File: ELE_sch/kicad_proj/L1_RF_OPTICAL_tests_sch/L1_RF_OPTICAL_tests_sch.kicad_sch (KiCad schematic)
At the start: 0 parts

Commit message: update parts list, schematics diode placement
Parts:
- added D1: BPW34S, OptoDevice:Osram_BPW34S-SMD, symbol Sensor_Optical:BPW34-SMD
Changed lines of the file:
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@@
 	(generator_version "10.0")
 	(paper "A4")
+	(symbol
+		(lib_id "Sensor_Optical:BPW34-SMD")
+		(at 145.288 92.456 0)
+		(unit 1)
+		(body_style 1)
+		(exclude_from_sim no)
+		(in_bom yes)
+		(on_board yes)
+		(in_pos_files yes)
+		(dnp no)
+		(fields_autoplaced yes)
+		(property "Reference" "D1"
+			(at 144.3609 83.82 0)
+			(show_name no)
+			(do_not_autoplace no)
+			(effects
+				(font
+					(size 1.27 1.27)
+				)
+			)
+		)
+		(property "Value" "BPW34S"
+			(at 144.3609 86.36 0)
+			(show_name no)
+			(do_not_autoplace no)
+			(effects
+				(font
+					(size 1.27 1.27)
+				)
+			)
+		)
+		(property "Footprint" "OptoDevice:Osram_BPW34S-SMD"
+			(at 145.288 88.011 0)
+			(hide yes)
+			(show_name no)
+			(do_not_autoplace no)
+			(effects
+				(font
+					(size 1.27 1.27)
+				)
+			)
+		)
+		(property "Datasheet" "https://dammedia.osram.info/media/resource/hires/osram-dam-5488319/BPW%2034%20S_EN.pdf"
+			(at 144.018 92.456 0)
+			(hide yes)
+			(show_name no)
+			(do_not_autoplace no)
+			(effects
+				(font
+					(size 1.27 1.27)
+				)
+			)
+		)
+		(property "Description" "Silicon PIN Photodiode, Area 2.65x2.65mm"
+			(at 145.288 92.456 0)
+			(hide yes)
+			(show_name no)
+			(do_not_autoplace no)
+			(effects
+				(font
+					(size 1.27 1.27)
+				)
+			)
+		)
+		(pin "1"
+		)
+		(pin "2"
+		)
+		(instances
+			(project "L1_RF_OPTICAL_tests_sch"
+				(path "/8a635b1b-9d9a-4020-b936-45919ee57615"
+					(reference "D1")
+					(unit 1)
+				)
+			)
+		)
+	)
 	(sheet_instances
 		(path "/"

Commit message: parts update
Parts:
- removed D1: BPW34S, OptoDevice:Osram_BPW34S-SMD, symbol Sensor_Optical:BPW34-SMD
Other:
- added sheet Optical laser transmitter (optical_laser_transmitter.kicad_sch)
- added sheet Optical receiver (optical_receiver.kicad_sch)
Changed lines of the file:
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@@
 	(generator_version "10.0")
 	(paper "A4")
-	(symbol
-		(lib_id "Sensor_Optical:BPW34-SMD")
-		(at 145.288 92.456 0)
-		(unit 1)
-		(body_style 1)
+	(sheet
+		(at 25.4 76.2)
+		(size 25.4 25.654)
 		(exclude_from_sim no)
 		(in_bom yes)
 		(on_board yes)
-		(in_pos_files yes)
 		(dnp no)
 		(fields_autoplaced yes)
-		(property "Reference" "D1"
-			(at 144.3609 83.82 0)
+		(stroke
+			(width 0.1524)
+			(type solid)
+		)
+		(fill
+			(color 0 0 0 0)
+		)
+		(property "Sheetname" "Optical receiver"
+			(at 25.4 75.4884 0)
 			(show_name no)
 			(do_not_autoplace no)
@@
 					(size 1.27 1.27)
 				)
+				(justify left bottom)
 			)
 		)
-		(property "Value" "BPW34S"
-			(at 144.3609 86.36 0)
+		(property "Sheetfile" "optical_receiver.kicad_sch"
+			(at 25.4 102.4386 0)
 			(show_name no)
 			(do_not_autoplace no)
@@
 					(size 1.27 1.27)
 				)
+				(justify left top)
 			)
 		)
-		(property "Footprint" "OptoDevice:Osram_BPW34S-SMD"
-			(at 145.288 88.011 0)
-			(hide yes)
+		(instances
+			(project "L1_RF_OPTICAL_tests_sch"
+				(path "/8a635b1b-9d9a-4020-b936-45919ee57615"
+					(page "2")
+				)
+			)
+		)
+	)
+	(sheet
+		(at 76.2 76.454)
+		(size 25.4 25.4)
+		(exclude_from_sim no)
+		(in_bom yes)
+		(on_board yes)
+		(dnp no)
+		(fields_autoplaced yes)
+		(stroke
+			(width 0.1524)
+			(type solid)
+		)
+		(fill
+			(color 0 0 0 0)
+		)
+		(property "Sheetname" "Optical laser transmitter"
+			(at 76.2 75.7424 0)
 			(show_name no)
 			(do_not_autoplace no)
@@
 					(size 1.27 1.27)
 				)
+				(justify left bottom)
 			)
 		)
-		(property "Datasheet" "https://dammedia.osram.info/media/resource/hires/osram-dam-5488319/BPW%2034%20S_EN.pdf"
-			(at 144.018 92.456 0)
-			(hide yes)
+		(property "Sheetfile" "optical_laser_transmitter.kicad_sch"
+			(at 76.2 102.4386 0)
 			(show_name no)
 			(do_not_autoplace no)
@@
 					(size 1.27 1.27)
 				)
+				(justify left top)
 			)
-		)
-		(property "Description" "Silicon PIN Photodiode, Area 2.65x2.65mm"
-			(at 145.288 92.456 0)
-			(hide yes)
-			(show_name no)
-			(do_not_autoplace no)
-			(effects
-				(font
-					(size 1.27 1.27)
-				)
-			)
-		)
-		(pin "1"
-		)
-		(pin "2"
 		)
 		(instances
 			(project "L1_RF_OPTICAL_tests_sch"
 				(path "/8a635b1b-9d9a-4020-b936-45919ee57615"
-					(reference "D1")
-					(unit 1)
+					(page "3")
 				)
 			)

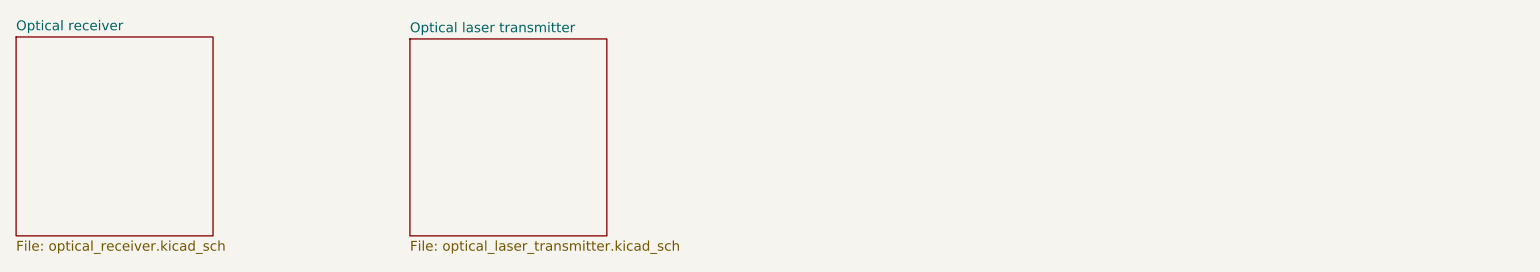
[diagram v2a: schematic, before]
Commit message: update microcontrollers settings, taksks list, RF and LED cricuiits
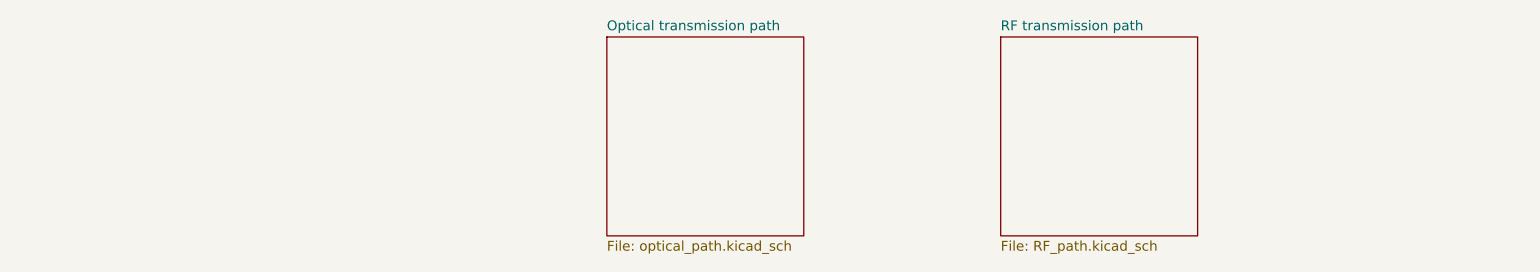
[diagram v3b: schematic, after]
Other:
- sheet Optical receiver renamed Optical transmission path
- removed sheet Optical laser transmitter
- added sheet RF transmission path (RF_path.kicad_sch)
- sheet Optical transmission path: file optical_receiver.kicad_sch -> optical_path.kicad_sch
- company: (none) -> by Wojciech Flis ®
- title: (none) -> Optical transmission path circuits
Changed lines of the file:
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@@
 	(generator_version "10.0")
 	(paper "A4")
+	(title_block
+		(title "Optical transmission path circuits")
+		(rev "v1.0")
+		(company "by Wojciech Flis ®")
+	)
 	(sheet
-		(at 25.4 76.2)
+		(at 101.6 76.2)
 		(size 25.4 25.654)
 		(exclude_from_sim no)
@@
 			(color 0 0 0 0)
 		)
-		(property "Sheetname" "Optical receiver"
-			(at 25.4 75.4884 0)
+		(property "Sheetname" "Optical transmission path"
+			(at 101.6 75.4884 0)
 			(show_name no)
 			(do_not_autoplace no)
@@
 			)
 		)
-		(property "Sheetfile" "optical_receiver.kicad_sch"
-			(at 25.4 102.4386 0)
+		(property "Sheetfile" "optical_path.kicad_sch"
+			(at 101.6 102.4386 0)
 			(show_name no)
 			(do_not_autoplace no)
@@
 	)
 	(sheet
-		(at 76.2 76.454)
-		(size 25.4 25.4)
+		(at 152.4 76.2)
+		(size 25.4 25.654)
 		(exclude_from_sim no)
 		(in_bom yes)
@@
 			(color 0 0 0 0)
 		)
-		(property "Sheetname" "Optical laser transmitter"
-			(at 76.2 75.7424 0)
+		(property "Sheetname" "RF transmission path"
+			(at 152.4 75.4884 0)
 			(show_name no)
 			(do_not_autoplace no)
@@
 			)
 		)
-		(property "Sheetfile" "optical_laser_transmitter.kicad_sch"
-			(at 76.2 102.4386 0)
+		(property "Sheetfile" "RF_path.kicad_sch"
+			(at 152.4 102.4386 0)
 			(show_name no)
 			(do_not_autoplace no)
@@
 			)
 		)
+		(property "Field2" ""
+			(at 152.4 76.2 0)
+			(hide yes)
+			(show_name no)
+			(do_not_autoplace no)
+			(effects
+				(font
+					(size 1.27 1.27)
+				)
+			)
+		)

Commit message: update of pinouts, schematics
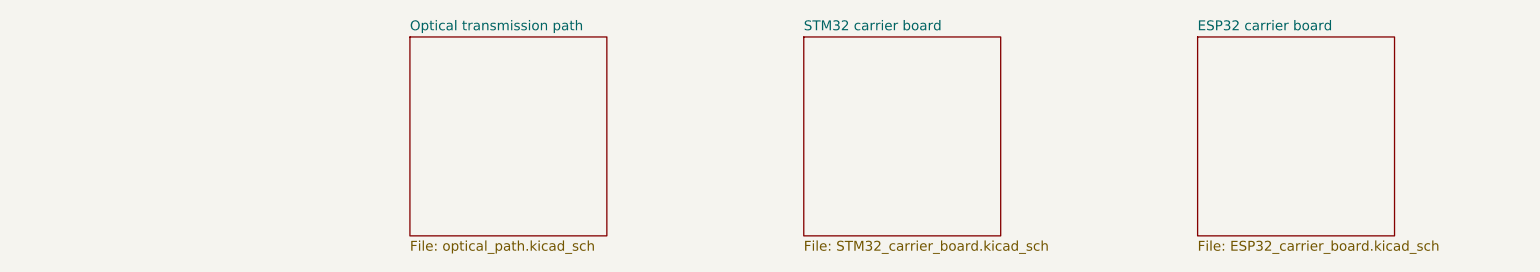
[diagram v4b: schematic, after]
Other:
- sheet RF transmission path renamed STM32 carrier board
- added sheet ESP32 carrier board (ESP32_carrier_board.kicad_sch)
- sheet STM32 carrier board: file RF_path.kicad_sch -> STM32_carrier_board.kicad_sch
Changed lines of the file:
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@@
 	)
 	(sheet
-		(at 101.6 76.2)
+		(at 76.2 76.2)
 		(size 25.4 25.654)
 		(exclude_from_sim no)
@@
 		)
 		(property "Sheetname" "Optical transmission path"
-			(at 101.6 75.4884 0)
+			(at 76.2 75.4884 0)
 			(show_name no)
 			(do_not_autoplace no)
@@
 		)
 		(property "Sheetfile" "optical_path.kicad_sch"
-			(at 101.6 102.4386 0)
+			(at 76.2 102.4386 0)
 			(show_name no)
 			(do_not_autoplace no)
@@
 	)
 	(sheet
-		(at 152.4 76.2)
+		(at 177.8 76.2)
 		(size 25.4 25.654)
 		(exclude_from_sim no)
@@
 			(color 0 0 0 0)
 		)
-		(property "Sheetname" "RF transmission path"
-			(at 152.4 75.4884 0)
+		(property "Sheetname" "ESP32 carrier board"
+			(at 177.8 75.4884 0)
 			(show_name no)
 			(do_not_autoplace no)
@@
 			)
 		)
-		(property "Sheetfile" "RF_path.kicad_sch"
-			(at 152.4 102.4386 0)
+		(property "Sheetfile" "ESP32_carrier_board.kicad_sch"
+			(at 177.8 102.4386 0)
 			(show_name no)
 			(do_not_autoplace no)
@@
 		)
 		(property "Field2" ""
-			(at 152.4 76.2 0)
+			(at 177.8 76.2 0)
 			(hide yes)
 			(show_name no)
+			(do_not_autoplace no)
+			(effects
+				(font
+					(size 1.27 1.27)
+				)
+			)
+		)
+		(instances
+			(project "L1_RF_OPTICAL_tests_sch"
+				(path "/8a635b1b-9d9a-4020-b936-45919ee57615"
+					(page "4")
+				)
+			)
+		)
+	)
+	(sheet
+		(at 127 76.2)
+		(size 25.4 25.654)
+		(exclude_from_sim no)
+		(in_bom yes)
+		(on_board yes)
+		(dnp no)
+		(fields_autoplaced yes)
+		(stroke
+			(width 0.1524)
+			(type solid)
+		)
+		(fill
+			(color 0 0 0 0)
+		)
+		(property "Sheetname" "STM32 carrier board"
+			(at 127 75.4884 0)
+			(show_name no)
+			(do_not_autoplace no)
+			(effects
+				(font
+					(size 1.27 1.27)
+				)
+				(justify left bottom)
+			)
+		)
+		(property "Sheetfile" "STM32_carrier_board.kicad_sch"
+			(at 127 102.4386 0)
+			(show_name no)
+			(do_not_autoplace no)
+			(effects
+				(font
+					(size 1.27 1.27)
+				)
+				(justify left top)
+			)
+		)
+		(property "Field2" ""
+			(at 127 76.2 0)
+			(hide yes)
+			(show_name no)
